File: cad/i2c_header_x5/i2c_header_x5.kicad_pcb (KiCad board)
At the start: 2 copper layers, 36.8 x 16.5 mm, 9 parts

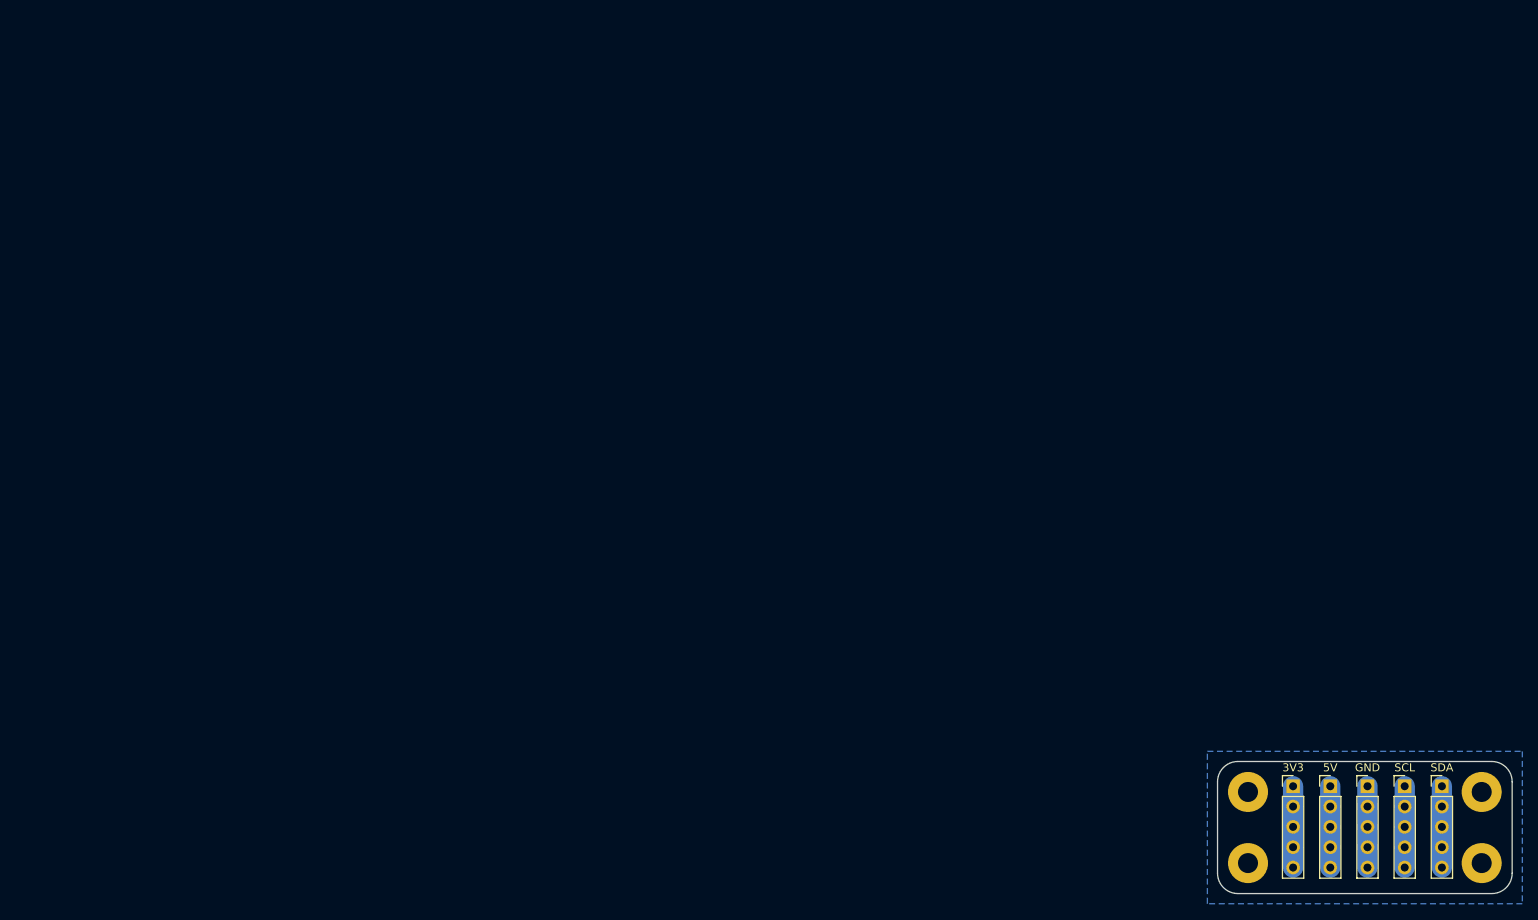
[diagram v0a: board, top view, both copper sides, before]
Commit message: Added SMD pull-up resistors to i2c header.
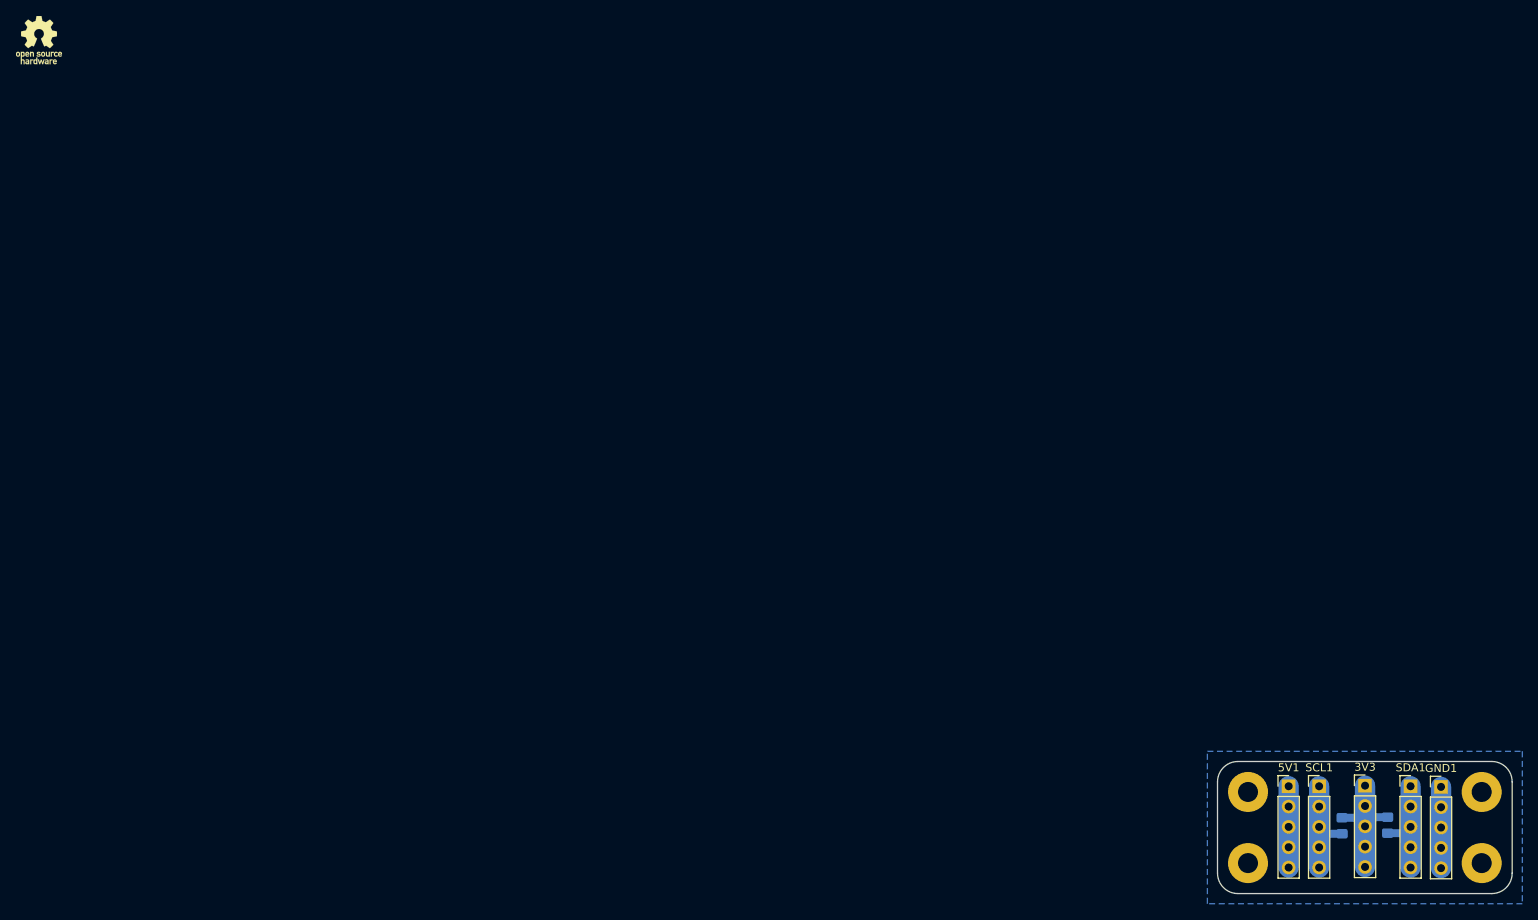
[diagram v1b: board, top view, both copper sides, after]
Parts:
- added R0: 4K7, Resistor_SMD:R_0805_2012Metric_Pad1.20x1.40mm_HandSolder, B.Cu at (168.6, 98.1)
- added R1: 4K7, Resistor_SMD:R_0805_2012Metric_Pad1.20x1.40mm_HandSolder, B.Cu at (162.9, 98.2)
- added REF**: OSHW-Logo_5.7x6mm_SilkScreen, Symbol:OSHW-Logo_5.7x6mm_SilkScreen, F.Cu at (0.00, 0.00)
- moved SCL1 10.7 mm to (160.0, 93.3)
- moved GND1 9.20 mm to (175.3, 93.3)
- moved 3V3 9.00 mm to (165.8, 93.2)
- moved 5V1 5.21 mm to (156.2, 93.3)
- moved SDA1 3.92 mm to (171.4, 93.3)
- renumbered 5V to 5V1, GND to GND1, SCL to SCL1, SDA to SDA1
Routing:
- net Net-(3V3-Pad1): track 10.2 -> 15.9 mm
- net Net-(R0-Pad1): track 10.2 -> 13.4 mm
- net Net-(R1-Pad1): track 10.2 -> 13.2 mm
